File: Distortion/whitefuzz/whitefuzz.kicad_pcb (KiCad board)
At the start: 2 copper layers, 52.6 x 29.9 mm, 27 parts, among them J1 Conn_01x04_Female, Q2 2n5088, Q3 2n5457

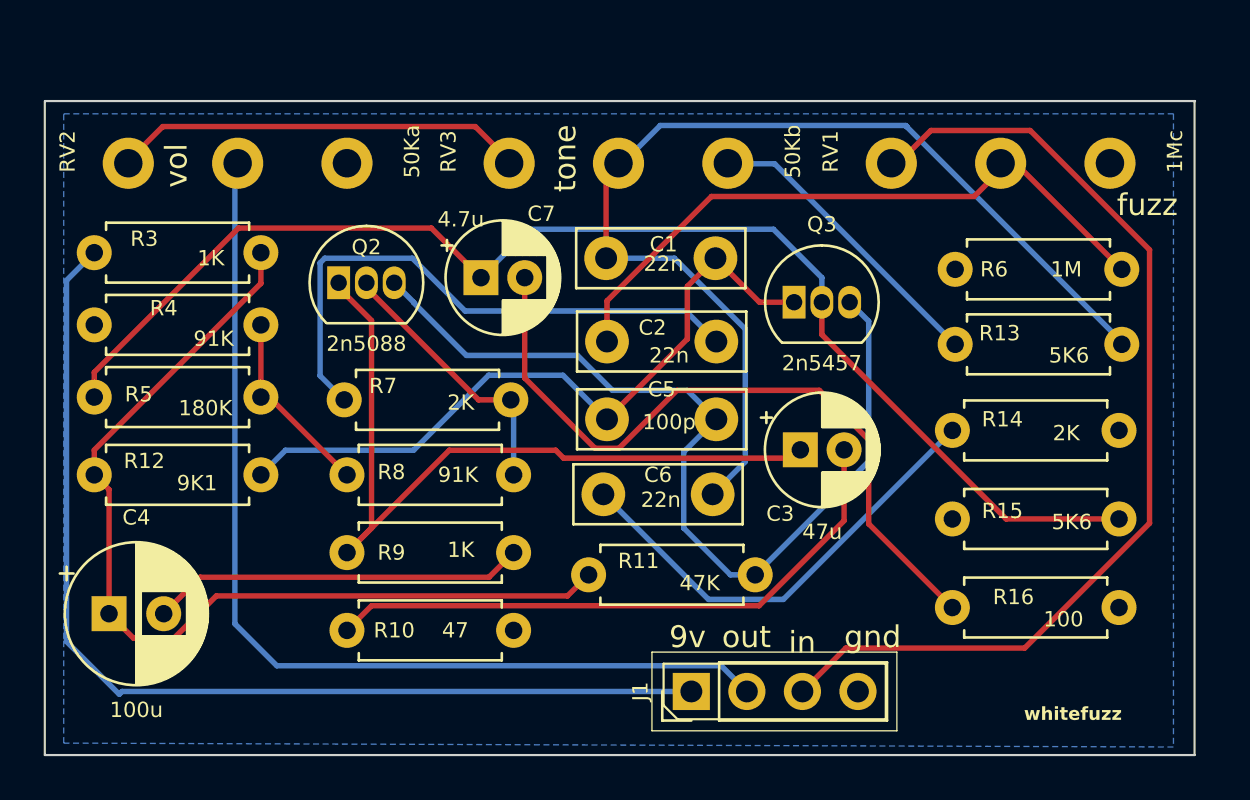
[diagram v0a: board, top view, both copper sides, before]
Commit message: replaced whiefuzz, and modified ejfuzzface
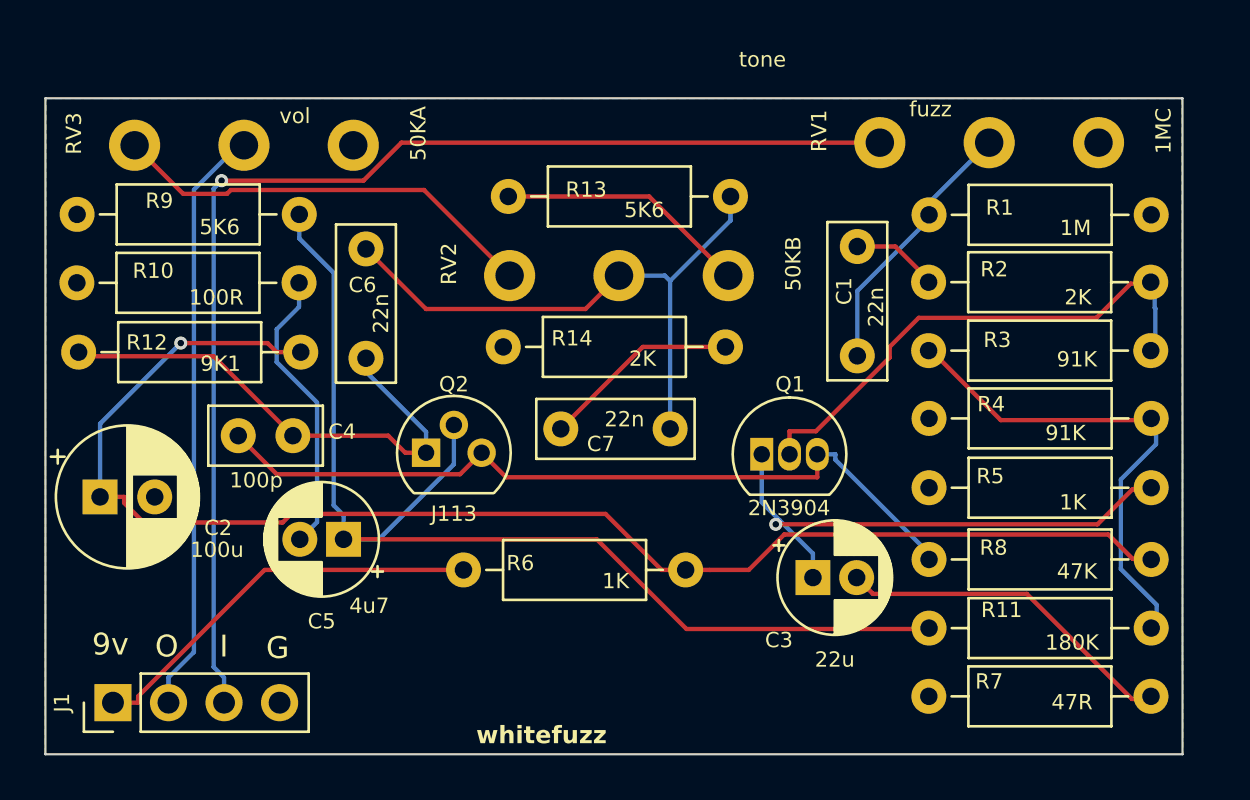
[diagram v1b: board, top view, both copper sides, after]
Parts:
- removed Q3: 2n5457, Package_TO_SOT_THT:TO-92_Inline
- removed R15: 5K6, Resistor_THT:R_Axial_DIN0207_L6.3mm_D2.5mm_P7.62mm_Horizontal
- removed R16: 100, Resistor_THT:R_Axial_DIN0207_L6.3mm_D2.5mm_P7.62mm_Horizontal
- added Q1: 2N3904, Package_TO_SOT_THT:TO-92_Inline, F.Cu at (132.8, 116.3)
- added R1: 1M, Resistor_THT:R_Axial_DIN0207_L6.3mm_D2.5mm_P10.16mm_Horizontal, F.Cu at (140.4, 105.3)
- added R2: 2K, Resistor_THT:R_Axial_DIN0207_L6.3mm_D2.5mm_P10.16mm_Horizontal, F.Cu at (140.4, 108.4)
- C1, C6: footprint Capacitor_THT:C_Disc_D7.5mm_W2.5mm_P5.00mm -> Capacitor_THT:C_Rect_L7.0mm_W2.5mm_P5.00mm
- C2: value 22n -> 100u; footprint Capacitor_THT:C_Disc_D7.5mm_W2.5mm_P5.00mm -> Capacitor_THT:CP_Radial_D6.3mm_P2.50mm
- C3: value 47u -> 22u
- C4: value 100u -> 100p; footprint Capacitor_THT:CP_Radial_D6.3mm_P2.50mm -> Capacitor_THT:C_Disc_D5.0mm_W2.5mm_P2.50mm
- C5: value 100p -> 4u7; footprint Capacitor_THT:C_Disc_D7.5mm_W2.5mm_P5.00mm -> Capacitor_THT:CP_Radial_D5.0mm_P2.00mm
- C7: value 4.7u -> 22n; footprint Capacitor_THT:CP_Radial_D5.0mm_P2.00mm -> Capacitor_THT:C_Rect_L7.0mm_W2.5mm_P5.00mm
- J1: value Conn_01x04_Female -> Conn_01x04_Pin
- Q2: value 2n5088 -> J113; footprint Package_TO_SOT_THT:TO-92_Inline -> Package_TO_SOT_THT:TO-92
- R10: value 47 -> 100R; footprint Resistor_THT:R_Axial_DIN0207_L6.3mm_D2.5mm_P7.62mm_Horizontal -> Resistor_THT:R_Axial_DIN0207_L6.3mm_D2.5mm_P10.16mm_Horizontal
- R11: value 47K -> 180K; footprint Resistor_THT:R_Axial_DIN0207_L6.3mm_D2.5mm_P7.62mm_Horizontal -> Resistor_THT:R_Axial_DIN0207_L6.3mm_D2.5mm_P10.16mm_Horizontal
- R12, R13, R14, R4: footprint Resistor_THT:R_Axial_DIN0207_L6.3mm_D2.5mm_P7.62mm_Horizontal -> Resistor_THT:R_Axial_DIN0207_L6.3mm_D2.5mm_P10.16mm_Horizontal
- R3: value 1K -> 91K; footprint Resistor_THT:R_Axial_DIN0207_L6.3mm_D2.5mm_P7.62mm_Horizontal -> Resistor_THT:R_Axial_DIN0207_L6.3mm_D2.5mm_P10.16mm_Horizontal
- R5: value 180K -> 1K; footprint Resistor_THT:R_Axial_DIN0207_L6.3mm_D2.5mm_P7.62mm_Horizontal -> Resistor_THT:R_Axial_DIN0207_L6.3mm_D2.5mm_P10.16mm_Horizontal
- R6: value 1M -> 1K; footprint Resistor_THT:R_Axial_DIN0207_L6.3mm_D2.5mm_P7.62mm_Horizontal -> Resistor_THT:R_Axial_DIN0207_L6.3mm_D2.5mm_P10.16mm_Horizontal
- R7: value 2K -> 47R; footprint Resistor_THT:R_Axial_DIN0207_L6.3mm_D2.5mm_P7.62mm_Horizontal -> Resistor_THT:R_Axial_DIN0207_L6.3mm_D2.5mm_P10.16mm_Horizontal
- R8: value 91K -> 47K; footprint Resistor_THT:R_Axial_DIN0207_L6.3mm_D2.5mm_P7.62mm_Horizontal -> Resistor_THT:R_Axial_DIN0207_L6.3mm_D2.5mm_P10.16mm_Horizontal
- R9: value 1K -> 5K6; footprint Resistor_THT:R_Axial_DIN0207_L6.3mm_D2.5mm_P7.62mm_Horizontal -> Resistor_THT:R_Axial_DIN0207_L6.3mm_D2.5mm_P10.16mm_Horizontal
- RV1: value 1Mc -> 1MC
- RV2: value 50Ka -> 50KB
- RV3: value 50Kb -> 50KA
- moved R3 38.4 mm to (140.4, 111.5)
- moved R4 38.4 mm to (140.4, 114.6)
- moved R5 38.4 mm to (140.4, 117.8)
- moved R7 30.0 mm to (140.4, 127.3)
- moved R8 26.9 mm to (140.4, 121.1)
- moved J1 26.5 mm to (103.1, 127.6)
- moved R6 26.4 mm to (119.1, 121.6)
- moved C2 24.2 mm to (102.5, 118.2)
- moved R13 21.5 mm to (121.2, 104.5)
- moved R14 20.9 mm to (120.9, 111.4)
- moved R10 20.1 mm to (101.4, 108.4)
- moved R9 19.8 mm to (101.5, 105.3)
- moved RV2 18.2 mm to (131.2, 108.1)
- moved RV3 17.1 mm to (114.1, 102.2)
- moved R11 15.8 mm to (140.4, 124.2)
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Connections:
- net IN renamed in
- C1 pad 2: Net-(Q3-D) -> Net-(C1-Pad2)
- C2 pad 1: Net-(C2-Pad1) -> vcc
- C2 pad 2: Net-(C2-Pad2) -> GND
- C3 pad 1: Net-(Q2-E) -> Net-(Q1-E)
- C4 pad 1: Net-(C4-Pad1) -> Net-(Q1-C)
- C4 pad 2: GND -> Net-(Q2-D)
- C5 pad 1: Net-(Q3-D) -> Net-(Q2-S)
- C5 pad 2: Net-(Q2-C) -> Net-(C5-Pad2)
- C6 pad 1: Net-(C6-Pad1) -> Net-(Q2-D)
- C6 pad 2: Net-(C1-Pad1) -> Net-(C6-Pad2)
- C7 pad 1: Net-(Q3-S) -> Net-(C7-Pad1)
- C7 pad 2: Net-(C7-Pad2) -> Net-(C6-Pad2)
- J1 pad 1: 9V -> +9V
- J1 pad 2: OUT -> out
- Q2 pad 1: Net-(Q2-E) -> Net-(Q2-D)
- Q2 pad 2: Net-(Q2-B) -> Net-(Q2-S)
- Q2 pad 3: Net-(Q2-C) -> Net-(Q1-C)
- R10 pad 1: Net-(C3-Pad2) -> GND
- R10 pad 2: GND -> Net-(C5-Pad2)
- R11 pad 1: Net-(C4-Pad1) -> Net-(Q2-S)
- R11 pad 2: Net-(Q2-C) -> Net-(R11-Pad2)
- R12 pad 1: Net-(C4-Pad1) -> Net-(Q2-D)
- R12 pad 2: Net-(Q3-D) -> vcc
- R13 pad 2: Net-(C1-Pad1) -> Net-(C6-Pad2)
- R14 pad 1: Net-(C6-Pad1) -> GND
- R14 pad 2: GND -> Net-(C7-Pad1)
- R3 pad 1: 9V -> Net-(R11-Pad2)
- R3 pad 2: Net-(C4-Pad1) -> Net-(Q1-B)
- R4 pad 2: Net-(R4-Pad2) -> Net-(R11-Pad2)
- R5 pad 1: Net-(Q3-S) -> GND
- R5 pad 2: Net-(R4-Pad2) -> Net-(Q1-E)
- R6 pad 1: GND -> +9V
- R6 pad 2: Net-(C2-Pad1) -> vcc
- R7 pad 1: Net-(C2-Pad2) -> GND
- R7 pad 2: Net-(Q2-B) -> Net-(C3-Pad2)
- R8 pad 1: Net-(R4-Pad2) -> Net-(Q1-C)
- R8 pad 2: Net-(Q2-B) -> vcc
- R9 pad 1: Net-(Q2-E) -> GND
- R9 pad 2: GND -> Net-(Q2-S)
- RV1 pad 2: Net-(C2-Pad1) -> Net-(C1-Pad1)
- RV2 pad 1: GND -> Net-(R13-Pad1)
- RV2 pad 2: OUT -> Net-(C6-Pad2)
- RV3 pad 1: Net-(R13-Pad1) -> GND
- RV3 pad 2: Net-(C1-Pad1) -> out
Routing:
- net vcc: track 0.00 -> 65.5 mm, vias 0 -> 1
- net Net-(Q3-S): track 59.6 -> 0.00 mm
- net Net-(Q2-S): track 0.00 -> 52.7 mm
- net 9V: track 47.9 -> 0.00 mm
- net OUT: track 45.7 -> 0.00 mm
- net Net-(C4-Pad1): track 43.5 -> 0.00 mm
- net Net-(Q2-C): track 42.1 -> 0.00 mm
- net Net-(Q1-C): track 0.00 -> 36.6 mm
- net Net-(Q2-E): track 36.4 -> 0.00 mm
- net Net-(C1-Pad1): track 48.3 -> 12.2 mm
- net Net-(C7-Pad2): track 32.9 -> 0.00 mm
- net Net-(Q3-D): track 32.4 -> 0.00 mm
- net Net-(C2-Pad1): track 30.0 -> 0.00 mm
- net Net-(C6-Pad2): track 0.00 -> 27.6 mm
- net out: track 0.00 -> 27.1 mm
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- added copper zone on F.Cu, net GND
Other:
- board size 52.6 x 29.9 mm -> 52 x 30 mm
- board text added: "G"
- board text added: "I"
- board text added: "O"
- board text removed: "gnd"
- board text removed: "in"
- board text removed: "out"
